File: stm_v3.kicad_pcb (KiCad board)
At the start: 4 copper layers, 60 x 41 mm, 55 parts, among them J1 OLED, J2 SWD, J3 OBDII, Q1 s8050, Q2 s8050, SW1 RST, SW2 BOOT0, U1 STM32L431RCTx, U2 SN65HVD231, U3 TPS562201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

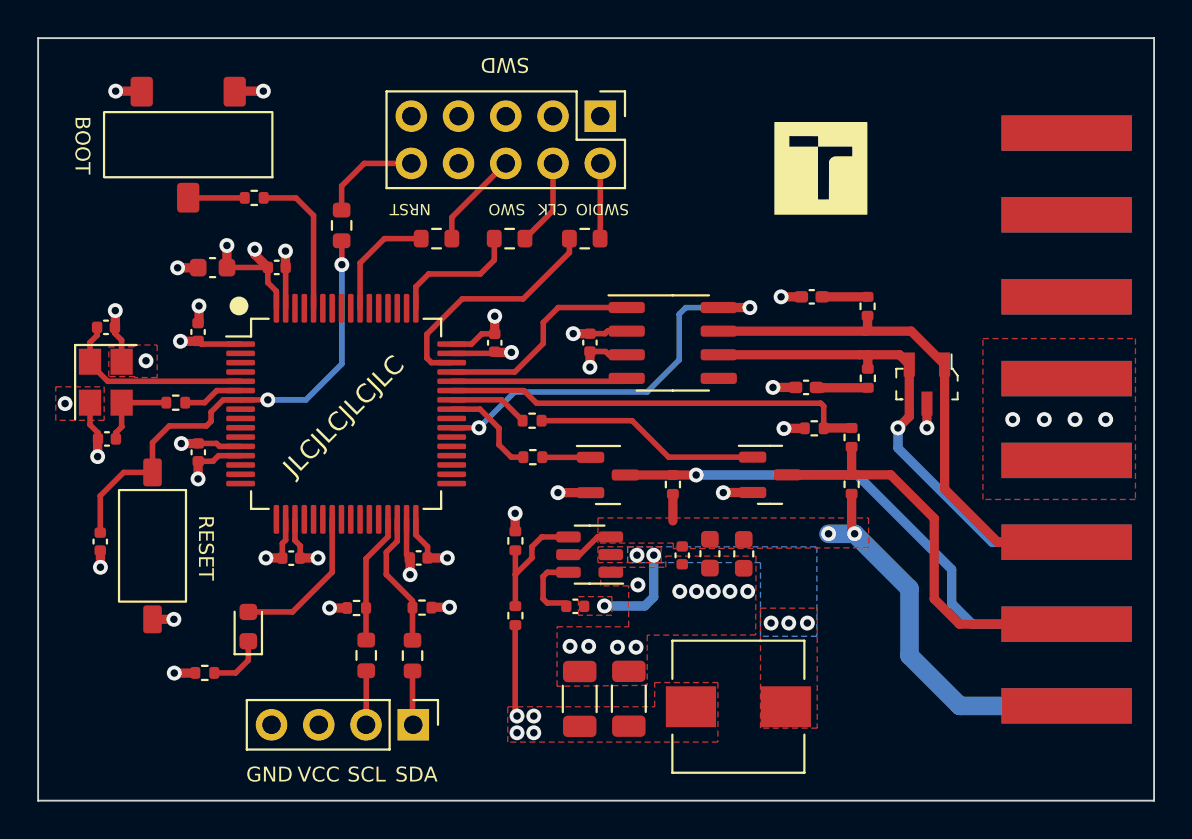
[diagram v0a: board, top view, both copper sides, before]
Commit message: Board v2 - reduced size
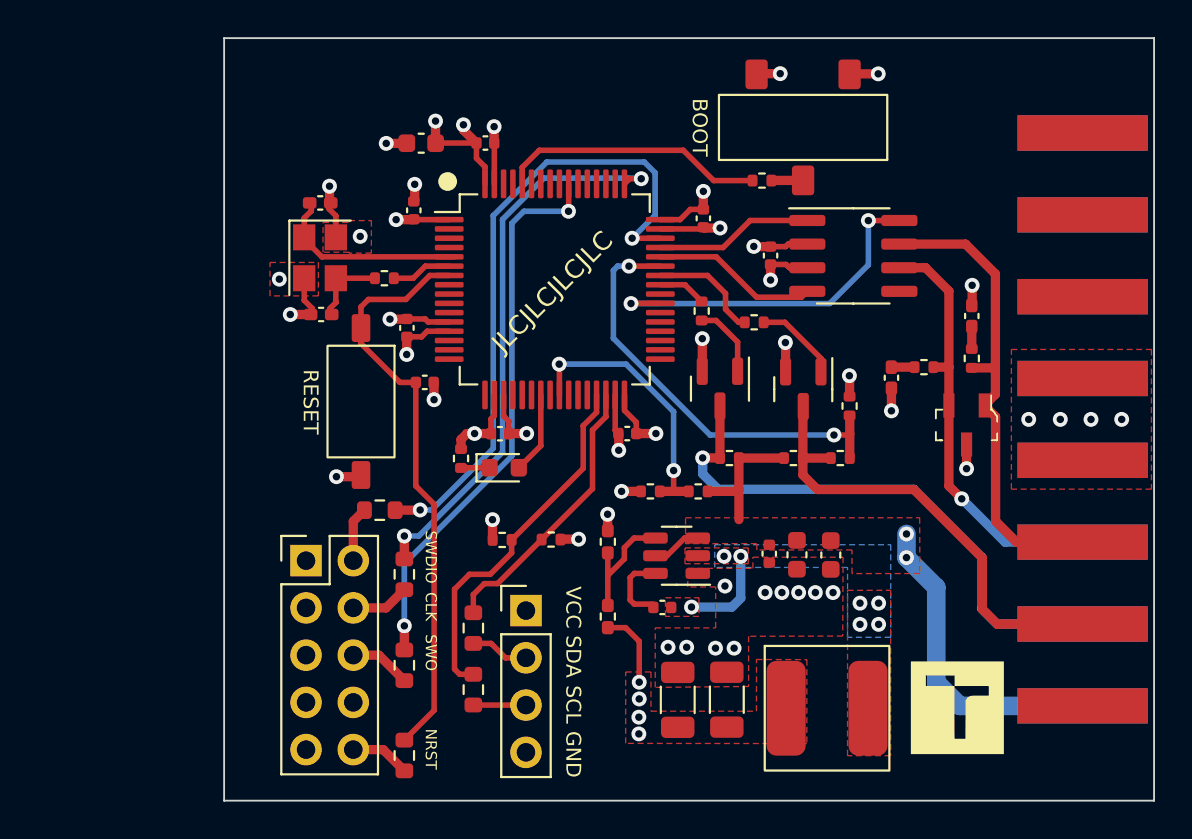
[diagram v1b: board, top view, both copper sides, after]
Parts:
- added R22: 100k, Resistor_SMD:R_0402_1005Metric, F.Cu at (161.1, 90.2)
- added R23: 27k, Resistor_SMD:R_0402_1005Metric, F.Cu at (158.5, 90.2)
- C8, C9: footprint Capacitor_SMD:C_0402_1005Metric -> Capacitor_SMD:C_0402_1005Metric_Pad0.74x0.62mm_HandSolder
- L1: footprint Inductor_SMD:L_Wuerth_HCI-7030 -> tme_library:VLS6045AF
- R13, R14: footprint Resistor_SMD:R_0402_1005Metric -> Resistor_SMD:R_0402_1005Metric_Pad0.72x0.64mm_HandSolder
- moved SW2 33.1 mm to (166.7, 70.6)
- moved G*** 29.9 mm to (175.0, 101.8)
- moved R10 28.7 mm to (145.3, 104.4), turned to 90 degrees
- moved J2 28.7 mm to (140.0, 93.9), turned to 0 degrees
- moved R4 27.3 mm to (164.5, 73.5), turned to 0 degrees
- moved R9 23.0 mm to (145.3, 99.5), turned to 90 degrees
- moved C10 19.4 mm to (146.4, 84.3), turned to 0 degrees
- moved R8 18.9 mm to (145.3, 94.6), turned to 90 degrees
- moved R7 18.3 mm to (144.0, 91.2), turned to 0 degrees
- moved R15 18.0 mm to (148.3, 88.4), turned to -90 degrees
- moved D2 16.2 mm to (150.7, 88.9), turned to 0 degrees
- moved SW1 13.6 mm to (143.0, 85.3)
- moved C8 13.3 mm to (140.8, 74.7)
- moved C9 13.3 mm to (140.8, 80.7)
- moved Y1 13.3 mm to (140.8, 77.6)
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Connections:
- J1 pad 1: /Connectors/SDA -> +3.3V
- J1 pad 2: /Connectors/SCL -> /Connectors/SDA
- J1 pad 3: +3.3V -> /Connectors/SCL
- U1 pad 25: unconnected-(U1-Pad25) -> BAT_V
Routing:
- net SWO: track 6.26 -> 30.1 mm, vias 0 -> 2
- net SWCLK: track 7.12 -> 30.3 mm, vias 0 -> 2
- net SWDIO: track 13.0 -> 34.9 mm, vias 0 -> 2
- net BAT_V: track 0.00 -> 14.6 mm, vias 0 -> 2
- net OLED_SCL: track 6.98 -> 19.7 mm
- net OLED_SDA: track 7.33 -> 15.1 mm
- net Net-(Q2-Pad1): track 12.2 -> 4.61 mm
- net BOOT0: track 8.06 -> 14.3 mm
- net NRST: track 25.8 -> 31.5 mm, vias 2 -> 0
- net CAN_L: track 27.1 -> 22.9 mm
- net LED: track 8.24 -> 4.40 mm
- net CAN_TX: track 11.5 -> 8.51 mm
- net LLine: track 5.45 -> 2.60 mm
- net ISO_K: track 22.4 -> 25.2 mm
- net CAN_S: track 21.8 -> 19.2 mm
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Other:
- board size 60 x 41 mm -> 50 x 41 mm
- board text removed: "SWD"

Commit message: Further board size reduction
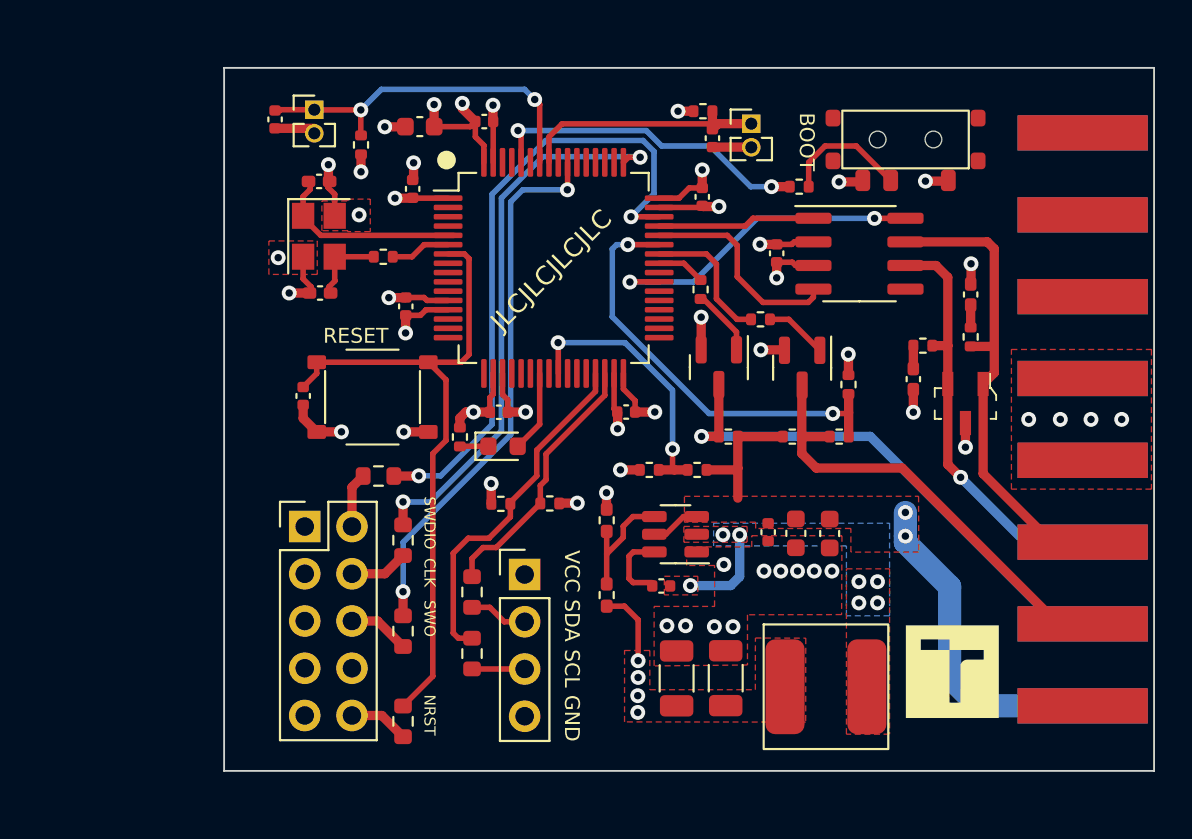
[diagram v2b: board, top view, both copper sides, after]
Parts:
- added C20: 100n, Capacitor_SMD:C_0402_1005Metric, F.Cu at (161.9, 71.2)
- added C21: 100n, Capacitor_SMD:C_0402_1005Metric, F.Cu at (138.3, 70.2)
- added R24: 4k7, Resistor_SMD:R_0402_1005Metric, F.Cu at (161.3, 69.7)
- added R25: 4k7, Resistor_SMD:R_0402_1005Metric, F.Cu at (143.0, 71.5)
- added SW3: LCD, Connector_PinHeader_1.27mm:PinHeader_1x02_P1.27mm_Vertical, F.Cu at (163.9, 70.4)
- added SW4: MENU, Connector_PinHeader_1.27mm:PinHeader_1x02_P1.27mm_Vertical, F.Cu at (140.4, 69.7)
- SW1: footprint tme_library:TS-1092S -> tme_library:XKB_TS_1187A
- SW2: footprint tme_library:XKB_SS-3235 -> tme_library:XKB_SS-3292S
- moved C10 6.58 mm to (139.8, 85.0), turned to -90 degrees
- moved SW2 5.55 mm to (172.2, 71.2)
- moved R4 2.03 mm to (166.5, 73.8)
- moved G*** 1.96 mm to (174.8, 99.9)
- moved R12 1.94 mm to (153.1, 90.8)
- moved J1 1.94 mm to (151.8, 94.6)
- moved R11 1.94 mm to (150.5, 90.8)
- moved R5 1.94 mm to (148.9, 95.6)
- moved R6 1.94 mm to (148.9, 98.9)
- moved R10 1.84 mm to (145.2, 102.5)
- moved R7 1.84 mm to (143.9, 89.3)
- moved J2 1.84 mm to (139.9, 92.1)
- moved R8 1.84 mm to (145.2, 92.8)
- moved R9 1.84 mm to (145.2, 97.7)
- moved C12 1.18 mm to (172.7, 84.1)
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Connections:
- net /BOOT_0 renamed /B_0
- U1 pad 57: unconnected-(U1-Pad57) -> LCD_BTN
- U1 pad 58: unconnected-(U1-Pad58) -> MENU_BTN
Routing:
- net MENU_BTN: track 0.00 -> 19.3 mm, vias 0 -> 2
- net LCD_BTN: track 0.00 -> 13.6 mm
- net GND: track 42.1 -> 47.6 mm
- net /B_0: track 1.70 -> 6.85 mm
- net NRST: track 31.5 -> 36.2 mm
- net BOOT0: track 14.3 -> 17.6 mm, vias 0 -> 2
- net CAN_RX: track 8.93 -> 11.3 mm
- net +3.3V: track 33.7 -> 35.6 mm, vias 15 -> 17
- net +12V: track 26.3 -> 27.8 mm
- net CAN_S: track 19.2 -> 17.8 mm
- net KLine_TX: track 6.08 -> 7.49 mm
- net Net-(Q2-Pad1): track 4.61 -> 3.37 mm
- net ISO_K: track 25.2 -> 24.1 mm
- net OLED_SDA: track 15.1 -> 14.3 mm
- net OLED_SCL: track 19.7 -> 18.9 mm
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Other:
- board size 50 x 41 mm -> 50 x 37.8 mm

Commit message: Final board version
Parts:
- moved G*** 1.63 mm to (175.4, 98.3)
- moved J3 0.71 mm to (181.1, 86.3)
- moved L1 0.43 mm to (167.9, 100.2)
- moved C1 0.19 mm to (146.3, 70.6)
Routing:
- net +12V: track 27.8 -> 24.3 mm
- net GND: track 47.6 -> 48.0 mm, vias 37 -> 36
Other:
- board size 50 x 37.8 mm -> 49 x 37.8 mm
- board text added: "LCD"
- board text added: "MENU"
